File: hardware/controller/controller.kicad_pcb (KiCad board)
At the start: 2 copper layers, 53.2 x 75.2 mm, 19 parts, among them U1 ESP32-S3-DEVKITC-1-N8R8

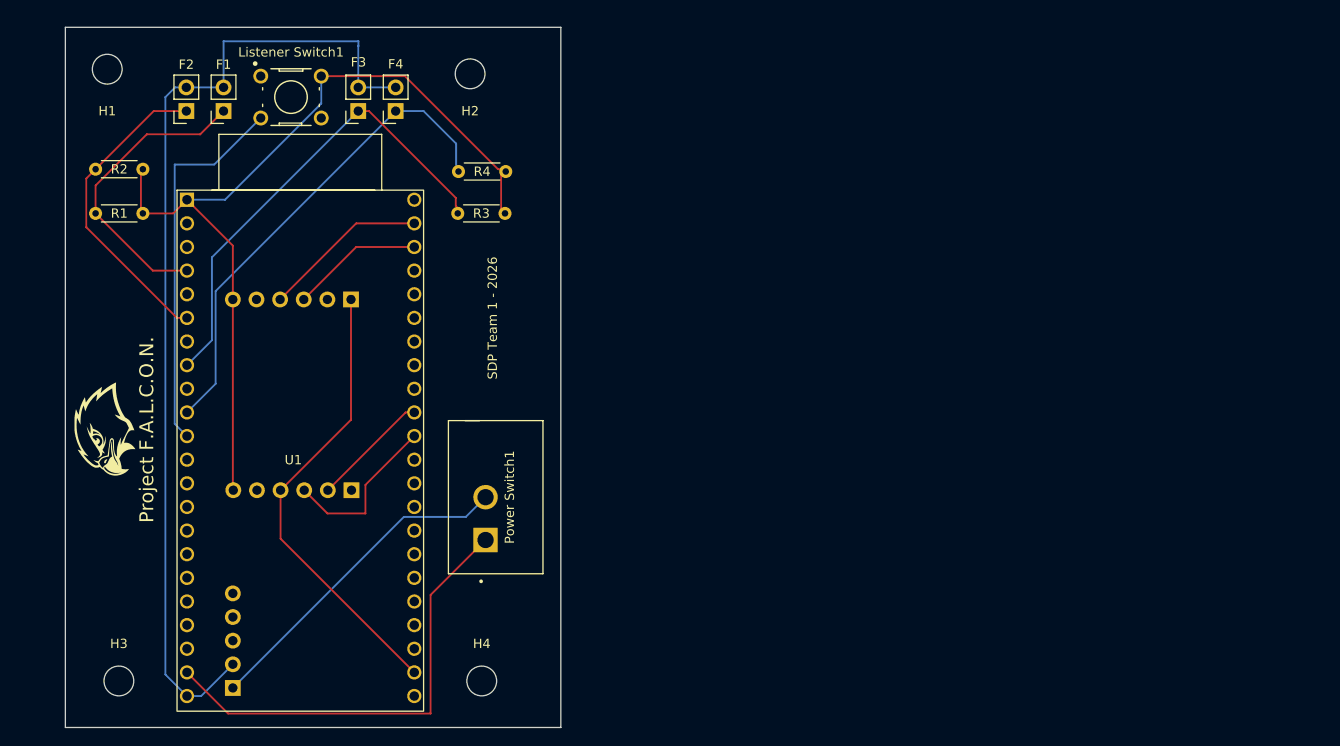
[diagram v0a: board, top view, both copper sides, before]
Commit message: kinda a shitshow, need to reroute after adding terminal blocks
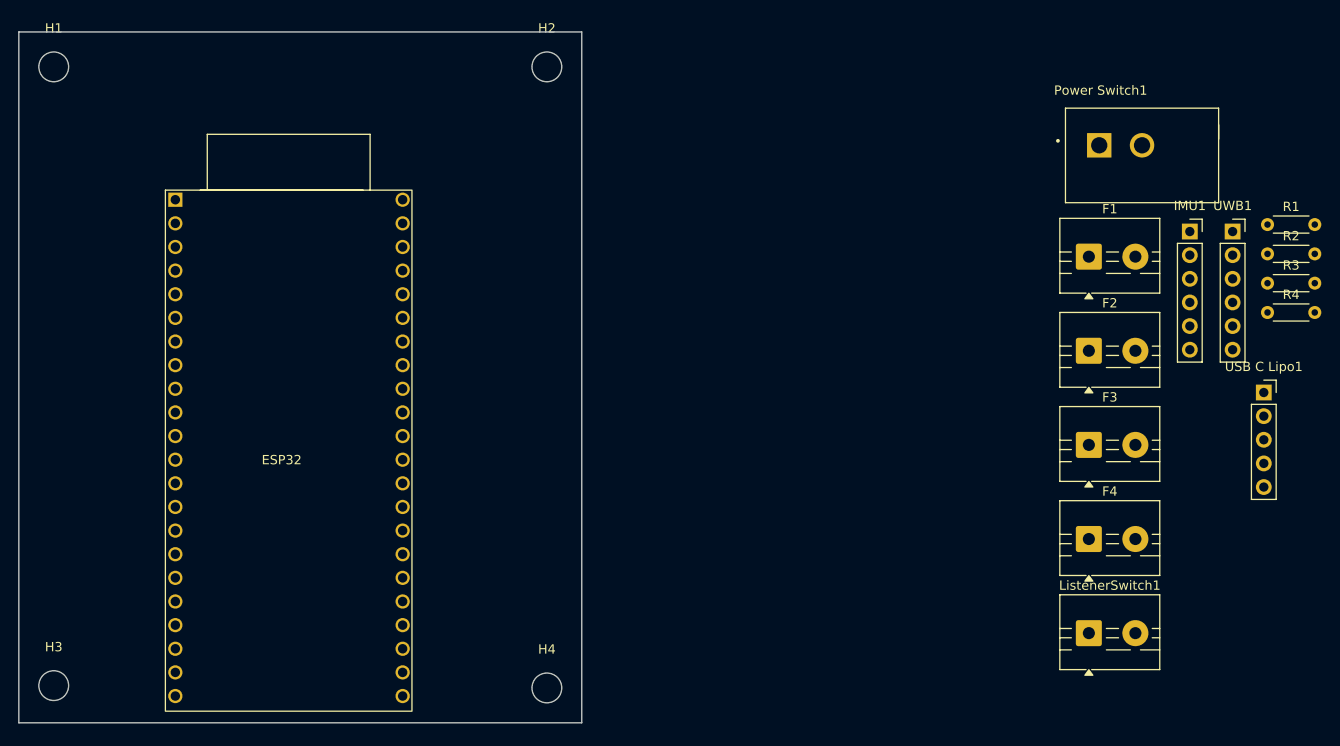
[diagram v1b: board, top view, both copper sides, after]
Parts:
- removed Listener Switch1: B3F-1000, Omron Tactile Button Small B3f-1000:SW_B3F-1000
- removed Project F.A.L.C.O.N.: LOGO, LOGO
- removed U1: ESP32-S3-DEVKITC-1-N8R8, SANXIXING ESP32-S3:ESP32-S3-DEVKITC-1-N8R8
- added ESP32: SANXIXING ESP32-S3, SANXIXING ESP32-S3:SANXIXING-ESP32-S3, F.Cu at (137.8, 102.0)
- added ListenerSwitch1: Screw_Terminal_01x02, TerminalBlock:TerminalBlock_MaiXu_MX126-5.0-02P_1x02_P5.00mm, F.Cu at (224.5, 118.6)
- F1, F2, F3, F4: value Conn_01x02_Pin -> Screw_Terminal_01x02; footprint Connector_PinSocket_2.54mm:PinSocket_1x02_P2.54mm_Vertical -> TerminalBlock:TerminalBlock_MaiXu_MX126-5.0-02P_1x02_P5.00mm
- IMU1, UWB1: moved to F.Cu
- USB C Lipo1: moved to F.Cu
- moved R2 126.3 mm to (243.7, 77.8)
- moved R1 126.0 mm to (243.7, 74.7)
- moved USB C Lipo1 115.3 mm to (243.3, 92.8)
- moved F2 100.4 mm to (224.5, 88.3), turned to 0 degrees
- moved UWB1 95.0 mm to (239.9, 75.5), turned to 0 degrees
- moved F1 94.3 mm to (224.5, 78.2), turned to 0 degrees
- moved IMU1 94.3 mm to (235.3, 75.5), turned to 0 degrees
- moved R4 88.3 mm to (243.7, 84.2)
- moved F4 87.6 mm to (224.5, 108.5), turned to 0 degrees
- moved F3 86.3 mm to (224.5, 98.4), turned to 0 degrees
- moved R3 82.3 mm to (243.7, 81.0), turned to 0 degrees
- moved Power Switch1 78.6 mm to (230.2, 67.3), turned to 0 degrees
- moved H2 8.28 mm to (166.2, 57.8)
- moved H4 7.04 mm to (166.2, 124.5)
- moved H3 7.02 mm to (113.2, 124.2)
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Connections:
- F2 pad 1: Net-(F2-Pin_1) -> Net-(F1-Pin_1)
- F2 pad 2: Net-(F1-Pin_2) -> Net-(F2-Pin_2)
- F3 pad 1: Net-(F3-Pin_1) -> Net-(F1-Pin_1)
- F3 pad 2: Net-(F1-Pin_2) -> Net-(F3-Pin_2)
- F4 pad 1: Net-(F4-Pin_1) -> Net-(F1-Pin_1)
- F4 pad 2: Net-(F1-Pin_2) -> Net-(F4-Pin_2)
- R1 pad 1: Net-(F1-Pin_1) -> Net-(F1-Pin_2)
- R2 pad 1: Net-(F2-Pin_1) -> Net-(F2-Pin_2)
- R3 pad 2: Net-(F3-Pin_1) -> Net-(F3-Pin_2)
- R4 pad 1: Net-(F4-Pin_1) -> Net-(F4-Pin_2)
- USB C Lipo1 pad 2: Net-(F1-Pin_2) -> Net-(F1-Pin_1)
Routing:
- net Net-(F1-Pin_2): track 106.8 -> 0.00 mm
- net Net-(IMU1-Pin_6): track 94.4 -> 0.00 mm
- net Net-(F4-Pin_1): track 52.7 -> 0.00 mm
- net Net-(F3-Pin_1): track 51.0 -> 0.00 mm
- net Net-(U1-5V0): track 49.3 -> 0.00 mm
- net Net-(IMU1-Pin_4): track 49.2 -> 0.00 mm
- net Net-(U1-GPIO18): track 41.0 -> 0.00 mm
- net Net-(USB C Lipo1-Pin_1): track 35.7 -> 0.00 mm
- net Net-(F2-Pin_1): track 33.8 -> 0.00 mm
- net Net-(F1-Pin_1): track 32.4 -> 0.00 mm
- net Net-(IMU1-Pin_3): track 18.1 -> 0.00 mm
- net Net-(U1-U0TXD/GPIO43): track 17.8 -> 0.00 mm
- net Net-(U1-U0RXD/GPIO44): track 14.2 -> 0.00 mm
- net Net-(IMU1-Pin_2): track 12.8 -> 0.00 mm
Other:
- board size 53.2 x 75.2 mm -> 60.5 x 74.2 mm
- board text removed: "SDP Team 1 - 2026"

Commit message: pcb placed, routed, designs and text added (DIMENSION CHECK NEEDED)
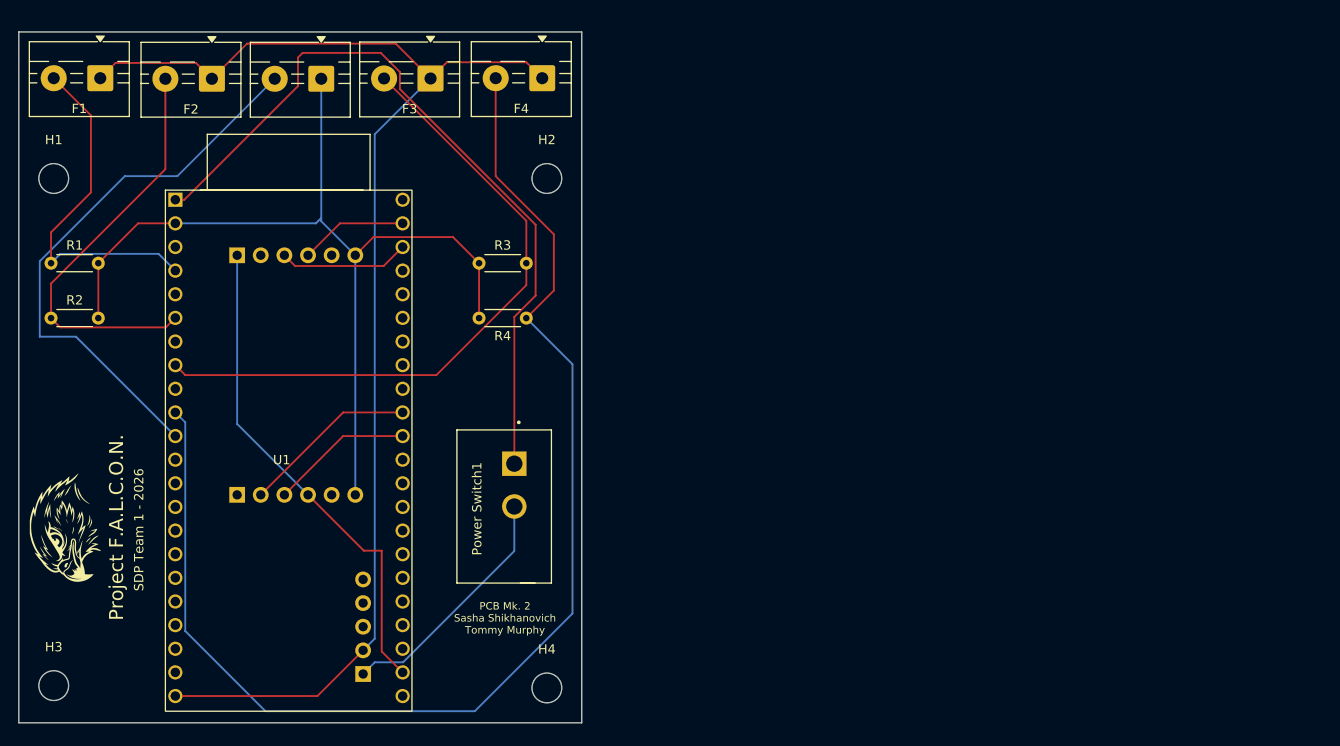
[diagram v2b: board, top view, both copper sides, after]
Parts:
- added Project F.A.L.C.O.N.: LOGO, LOGO, F.Cu at (114.5, 107.2)
- IMU1, UWB1: moved to B.Cu
- USB C Lipo1: moved to B.Cu
- moved R2 130.9 mm to (113.0, 84.8)
- moved R1 130.8 mm to (113.0, 78.8)
- moved F1 108.0 mm to (118.2, 59.0), turned to 180 degrees
- moved UWB1 107.0 mm to (133.0, 78.0), turned to -90 degrees
- moved IMU1 106.2 mm to (133.0, 103.8), turned to -90 degrees
- moved ListenerSwitch1 101.8 mm to (142.0, 59.0), turned to 180 degrees
- moved USB C Lipo1 101.4 mm to (146.5, 123.0)
- moved F2 98.7 mm to (130.2, 59.0), turned to 180 degrees
- moved R3 84.8 mm to (159.0, 78.8)
- moved F3 81.0 mm to (153.8, 59.0), turned to 180 degrees
- moved R4 79.7 mm to (164.0, 84.8), turned to 180 degrees
- moved Power Switch1 78.3 mm to (161.7, 105.0), turned to -90 degrees
- moved F4 76.8 mm to (165.8, 59.0), turned to 180 degrees
- moved H1 12.0 mm to (113.2, 69.8)
- moved H2 12.0 mm to (166.2, 69.8)
- renumbered ESP32 to U1
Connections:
- Power Switch1 pad 1: Net-(U1-5V0) -> Net-(U1-3V3)
- U1 pad J1_1: Net-(IMU1-Pin_6) -> Net-(U1-3V3)
- U1 pad J1_2: unconnected-(U1-3V3.-PadJ1_2) -> Net-(IMU1-Pin_6)
- U1 pad J1_21: Net-(U1-5V0) -> unconnected-(U1-5V0-PadJ1_21)
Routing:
- net Net-(F1-Pin_1): track 0.00 -> 140.1 mm
- net Net-(F4-Pin_2): track 0.00 -> 136.9 mm
- net Net-(IMU1-Pin_6): track 0.00 -> 99.3 mm
- net Net-(U1-3V3): track 0.00 -> 82.4 mm
- net Net-(F3-Pin_2): track 0.00 -> 70.7 mm
- net Net-(ListenerSwitch1-Pin_2): track 0.00 -> 60.5 mm
- net Net-(IMU1-Pin_4): track 0.00 -> 53.3 mm
- net Net-(F2-Pin_2): track 0.00 -> 45.0 mm
- net Net-(F1-Pin_2): track 0.00 -> 37.8 mm
- net Net-(USB C Lipo1-Pin_1): track 0.00 -> 26.5 mm
- net Net-(IMU1-Pin_2): track 0.00 -> 18.9 mm
- net Net-(IMU1-Pin_3): track 0.00 -> 15.3 mm
- net Net-(U1-U0RXD/GPIO44): track 0.00 -> 14.0 mm
- net Net-(U1-U0TXD/GPIO43): track 0.00 -> 11.6 mm
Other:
- board text added: "PCB Mk. 2 Sasha Shikhanovich Tommy Murphy"
- board text added: "SDP Team 1 - 2026"

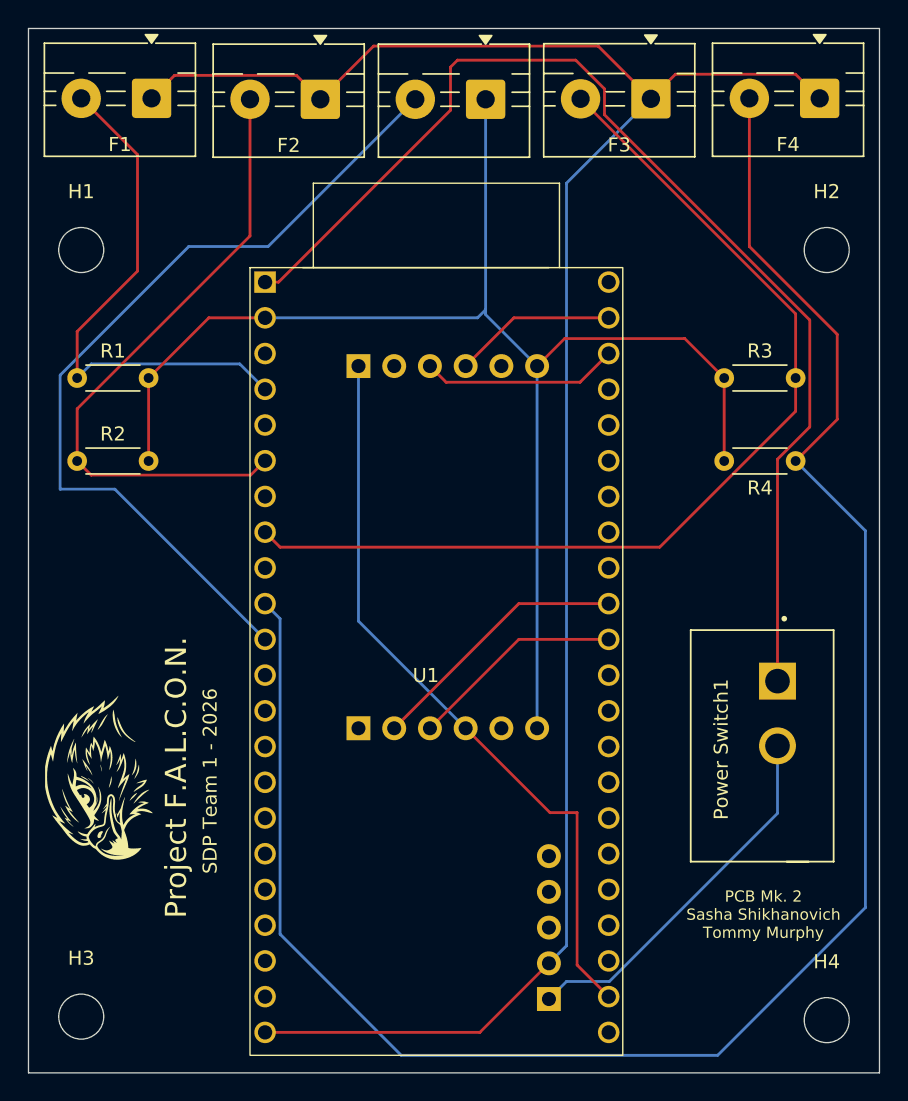
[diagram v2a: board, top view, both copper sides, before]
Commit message: routing and placing checkpoint, should be ready for fab
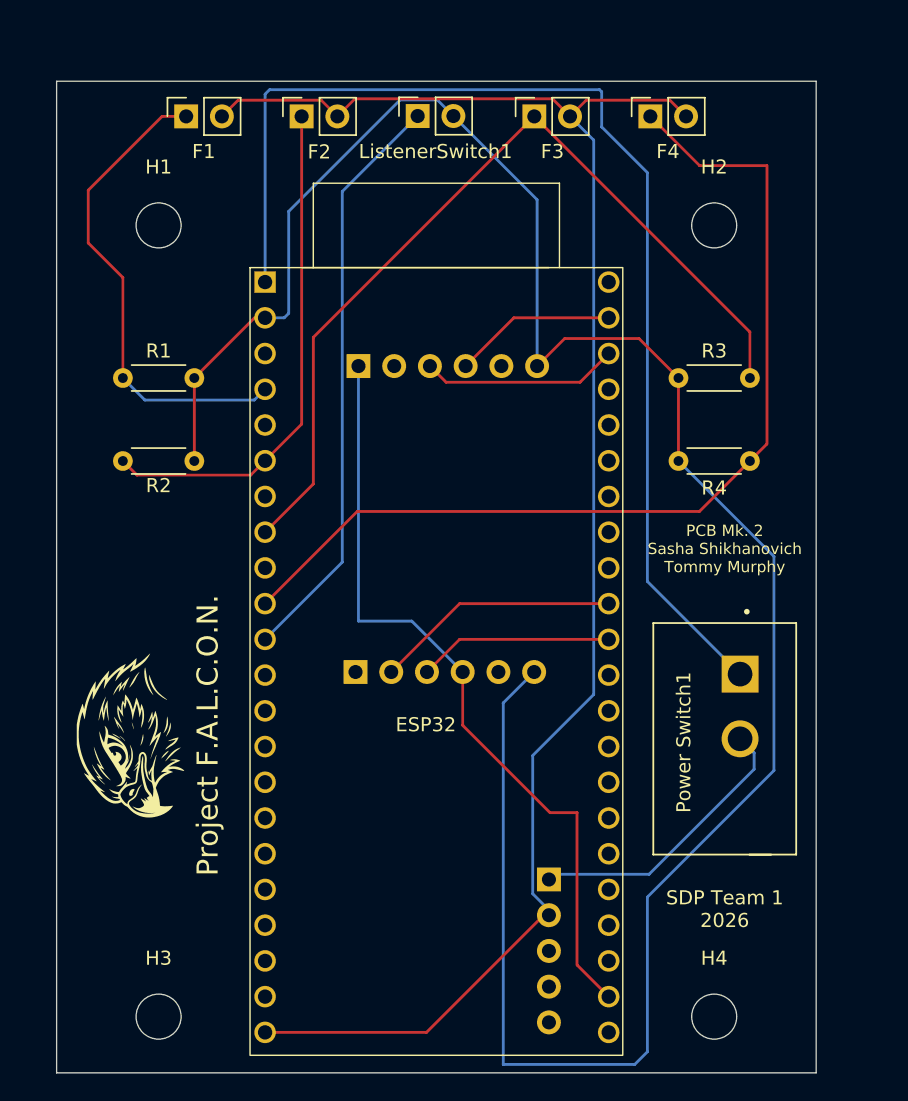
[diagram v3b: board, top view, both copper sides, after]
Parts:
- F1, F2, F3, F4, ListenerSwitch1: value Screw_Terminal_01x02 -> Conn_01x02_Pin; footprint TerminalBlock:TerminalBlock_MaiXu_MX126-5.0-02P_1x02_P5.00mm -> Connector_PinSocket_2.54mm:PinSocket_1x02_P2.54mm_Vertical
- moved F4 12.1 mm to (153.7, 60.2), turned to 90 degrees
- moved USB C Lipo1 8.50 mm to (146.5, 114.5), turned to 180 degrees
- moved F3 8.38 mm to (145.5, 60.2), turned to 90 degrees
- moved H2 8.19 mm to (158.2, 68.0)
- moved H4 8.00 mm to (158.2, 124.2)
- moved H1 5.77 mm to (118.8, 68.0)
- moved H3 5.50 mm to (118.8, 124.2)
- moved ListenerSwitch1 4.98 mm to (137.2, 60.2), turned to 90 degrees
- moved IMU1 4.01 mm to (132.8, 99.8)
- moved Project F.A.L.C.O.N. 3.75 mm to (116.8, 104.2)
- moved R1 3.25 mm to (116.2, 78.8)
- moved R2 3.25 mm to (116.2, 84.8)
- moved R3 3.25 mm to (155.7, 78.8)
- moved R4 3.25 mm to (160.8, 84.8)
- moved F1 2.77 mm to (120.7, 60.2), turned to 90 degrees
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- renumbered U1 to ESP32
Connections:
- ESP32 pad J1_10: Net-(F4-Pin_2) -> Net-(F4-Pin_1)
- ESP32 pad J1_11: Net-(ListenerSwitch1-Pin_2) -> Net-(ListenerSwitch1-Pin_1)
- ESP32 pad J1_22: Net-(F1-Pin_1) -> Net-(F1-Pin_2)
- ESP32 pad J1_4: Net-(F1-Pin_2) -> Net-(F1-Pin_1)
- ESP32 pad J1_6: Net-(F2-Pin_2) -> Net-(F2-Pin_1)
- ESP32 pad J1_8: Net-(F3-Pin_2) -> Net-(F3-Pin_1)
- F2 pad 1: Net-(F1-Pin_1) -> Net-(F2-Pin_1)
- F2 pad 2: Net-(F2-Pin_2) -> Net-(F1-Pin_2)
- F3 pad 1: Net-(F1-Pin_1) -> Net-(F3-Pin_1)
- F3 pad 2: Net-(F3-Pin_2) -> Net-(F1-Pin_2)
- F4 pad 1: Net-(F1-Pin_1) -> Net-(F4-Pin_1)
- F4 pad 2: Net-(F4-Pin_2) -> Net-(F1-Pin_2)
- ListenerSwitch1 pad 1: Net-(IMU1-Pin_6) -> Net-(ListenerSwitch1-Pin_1)
- ListenerSwitch1 pad 2: Net-(ListenerSwitch1-Pin_2) -> Net-(IMU1-Pin_6)
- R1 pad 1: Net-(F1-Pin_2) -> Net-(F1-Pin_1)
- R2 pad 1: Net-(F2-Pin_2) -> Net-(F2-Pin_1)
- R3 pad 2: Net-(F3-Pin_2) -> Net-(F3-Pin_1)
- R4 pad 1: Net-(F4-Pin_2) -> Net-(F4-Pin_1)
- USB C Lipo1 pad 2: Net-(F1-Pin_1) -> Net-(F1-Pin_2)
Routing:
- net Net-(F4-Pin_2): track 136.9 -> 0.00 mm
- net Net-(F1-Pin_1): track 140.1 -> 34.6 mm
- net Net-(F1-Pin_2): track 37.8 -> 119.3 mm
- net Net-(F3-Pin_2): track 70.7 -> 0.00 mm
- net Net-(F4-Pin_1): track 0.00 -> 69.9 mm
- net Net-(IMU1-Pin_6): track 99.3 -> 163.7 mm
- net Net-(F3-Pin_1): track 0.00 -> 62.4 mm
- net Net-(ListenerSwitch1-Pin_2): track 60.5 -> 0.00 mm
- net Net-(F2-Pin_2): track 45.0 -> 0.00 mm
- net Net-(ListenerSwitch1-Pin_1): track 0.00 -> 41.7 mm
- net Net-(F2-Pin_1): track 0.00 -> 36.5 mm
- net Net-(USB C Lipo1-Pin_1): track 26.5 -> 20.4 mm
- net Net-(IMU1-Pin_4): track 53.3 -> 55.5 mm
- net Net-(IMU1-Pin_3): track 15.3 -> 13.9 mm
- net Net-(IMU1-Pin_2): track 18.9 -> 17.5 mm
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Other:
- board size 60.5 x 74.2 mm -> 54 x 70.5 mm
- board text added: "SDP Team 1 2026"
- board text removed: "SDP Team 1 - 2026"
